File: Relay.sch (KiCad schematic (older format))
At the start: 0 parts

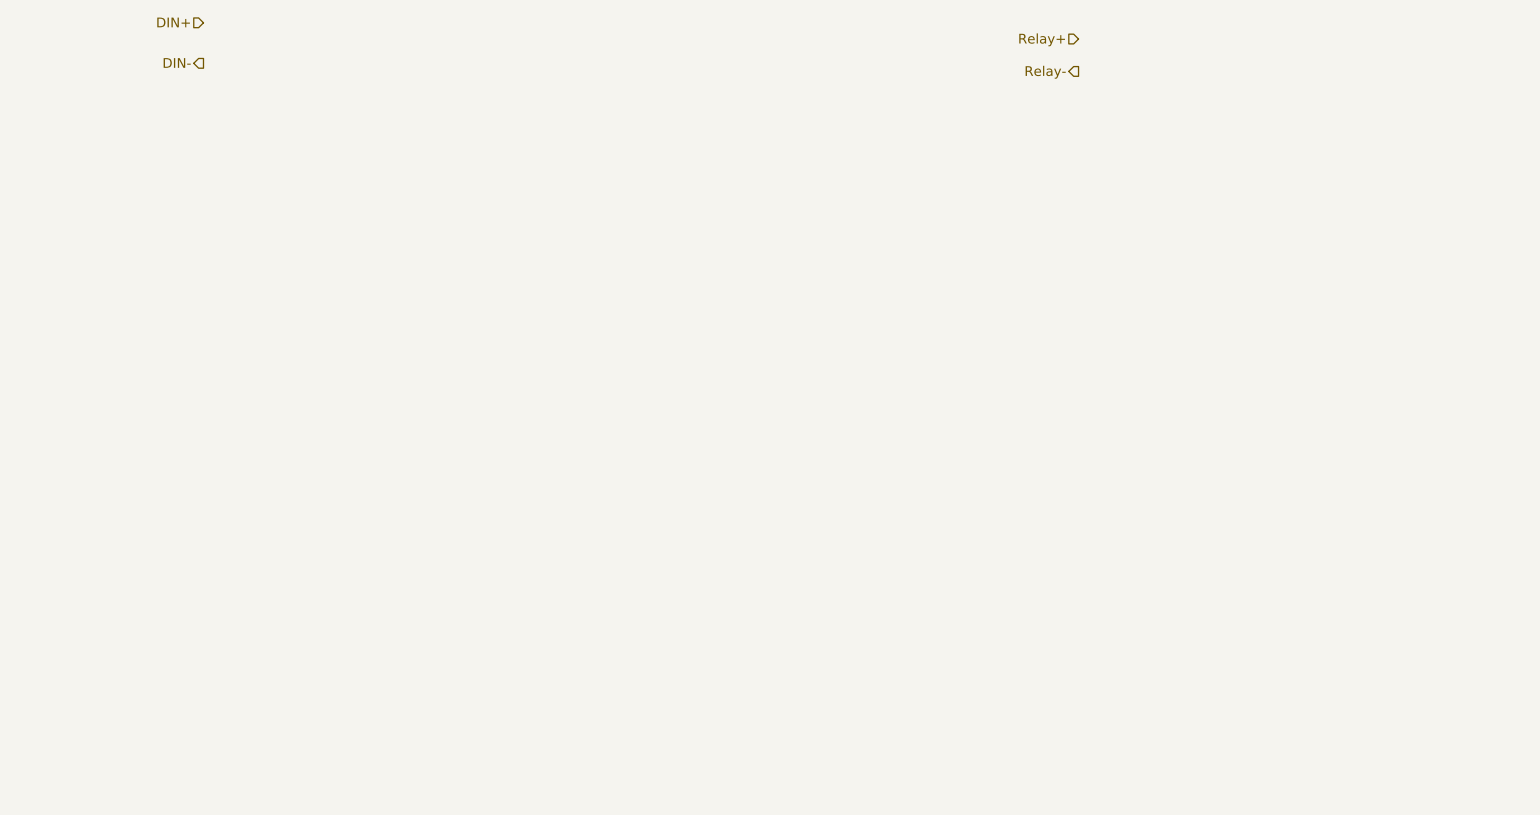
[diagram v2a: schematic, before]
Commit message: Completed LED Driver Video + Power Module
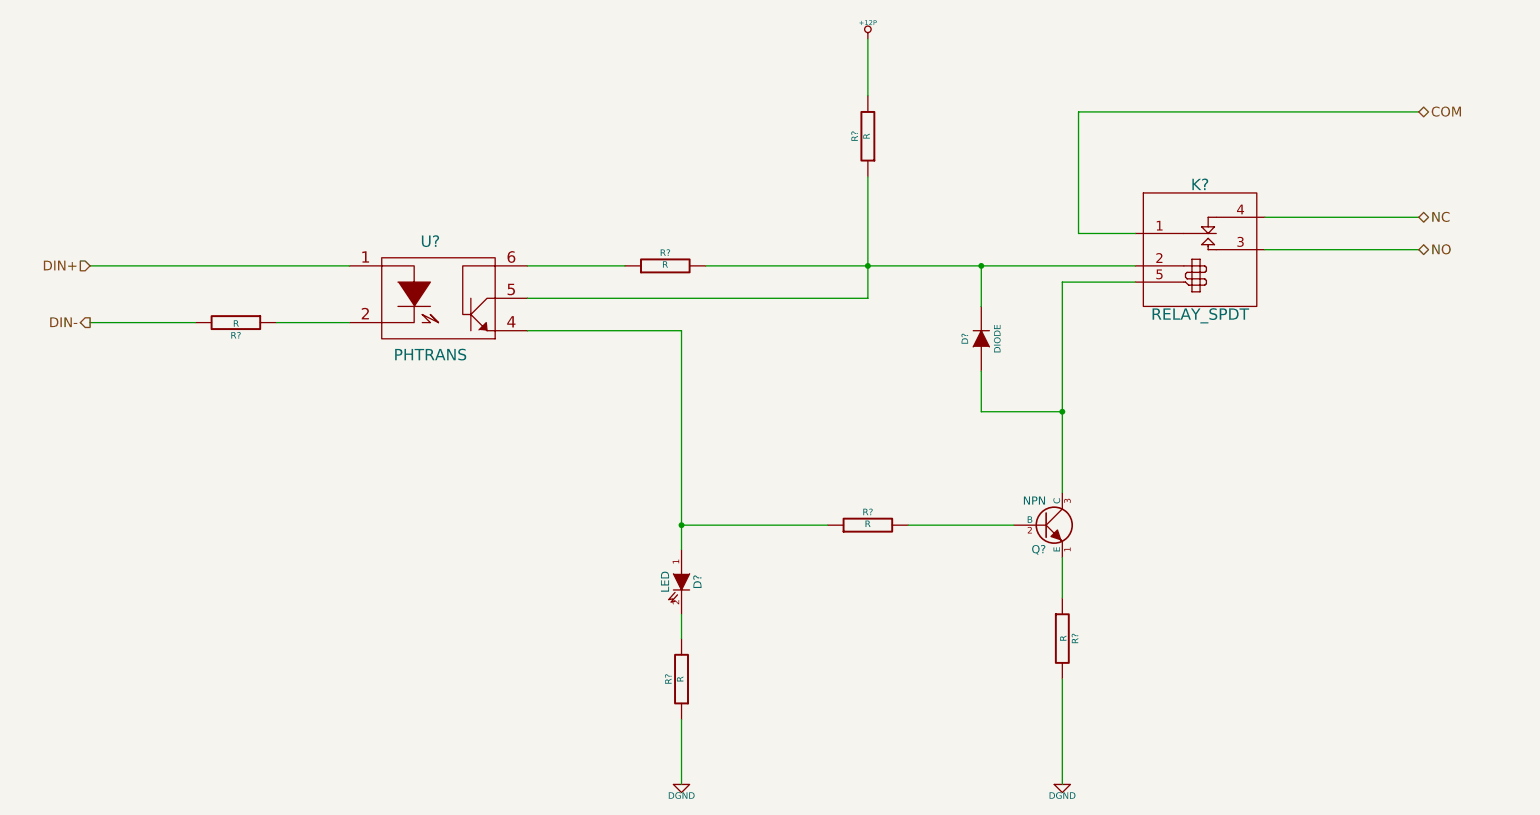
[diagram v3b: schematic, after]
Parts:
- added D?: LED, ~, symbol LED
- added D?: DIODE, ~, symbol DIODE
- added K?: RELAY_SPDT, ~, symbol RELAY_SPDT
- added Q?: NPN, ~, symbol NPN
- added R? (x6): R, ~, symbol R
- added U?: PHTRANS, ~, symbol PHTRANS
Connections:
- net DIN+: now also U?.1
- net DIN-: now also R?.2
- new net: R?.1, U?.2
- new net: D?.1 (A), R?.1, U?.4
- new net: D?.2 (K), K?.2 (COIL+), R?.1, R?.2, U?.5
- new net: R?.1, U?.6
- new net: Q?.2 (B), R?.2
- new net: Q?.1 (E), R?.1
- new net: D?.1 (A), K?.5 (COIL-), Q?.3 (C)
- new net: D?.2 (K), R?.2
- new net +12P: R?.2
- new net COM: K?.1 (COM)
- new net DGND: R?.1, R?.2
- new net NC: K?.4 (NC)
- new net NO: K?.3 (NO)
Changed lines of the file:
@@
 LIBS:contrib
 LIBS:valves
+LIBS:BenchBudEE_Parts
 LIBS:BenchBudEE-cache
 EELAYER 27 0
@@
 $Descr A4 11693 8268
 encoding utf-8
-Sheet 4 8
+Sheet 8 9
 Title ""
-Date "6 feb 2014"
+Date "10 feb 2014"
 Rev ""
 Comp ""
@@
 Comment4 ""
 $EndDescr
-Text HLabel 2250 2050 0    60   Input ~ 0
+Text HLabel 1550 3550 0    60   Input ~ 0
 DIN+
-Text HLabel 2250 2300 0    60   Output ~ 0
+Text HLabel 1550 3900 0    60   Output ~ 0
 DIN-
-Text HLabel 7650 2150 0    60   Input ~ 0
-Relay+
-Text HLabel 7650 2350 0    60   Output ~ 0
-Relay-
+Text HLabel 9750 3450 2    60   BiDi ~ 0
+NO
+Text HLabel 9750 3250 2    60   BiDi ~ 0
+NC
+$Comp
+L PHTRANS U?
+U 1 1 52F65C85
+P 3700 3750
+F 0 "U?" H 3650 4100 70  0000 C CNN
+F 1 "PHTRANS" H 3650 3400 70  0000 C CNN
+F 2 "~" H 3700 3750 60  0000 C CNN
+F 3 "~" H 3700 3750 60  0000 C CNN
+	1    3700 3750
+	1    0    0    -1
+$EndComp
+$Comp
+L R R?
+U 1 1 52F65C9E
+P 6350 5150
+F 0 "R?" V 6430 5150 40  0000 C CNN
+F 1 "R" V 6357 5151 40  0000 C CNN
+F 2 "~" V 6280 5150 30  0000 C CNN
+F 3 "~" H 6350 5150 30  0000 C CNN
+	1    6350 5150
+	0    -1   -1   0
+$EndComp
+$Comp
+L NPN Q?
+U 1 1 52F65CAD
+P 7450 5150
+F 0 "Q?" H 7450 5000 50  0000 R CNN
+F 1 "NPN" H 7450 5300 50  0000 R CNN
+F 2 "~" H 7450 5150 60  0000 C CNN
+F 3 "~" H 7450 5150 60  0000 C CNN
+	1    7450 5150
+	1    0    0    -1
+$EndComp
+$Comp
+L LED D?
+U 1 1 52F65CBC
+P 5200 5500
+F 0 "D?" H 5200 5600 50  0000 C CNN
+F 1 "LED" H 5200 5400 50  0000 C CNN
+F 2 "~" H 5200 5500 60  0000 C CNN
+F 3 "~" H 5200 5500 60  0000 C CNN
+	1    5200 5500
+	0    1    1    0
+$EndComp
+$Comp
+L RELAY_SPDT K?
+U 1 1 52F663F3
+P 8400 3300
+F 0 "K?" H 8400 3550 70  0000 C CNN
+F 1 "RELAY_SPDT" H 8400 2750 70  0000 C CNN
+F 2 "~" H 8400 3300 60  0000 C CNN
+F 3 "~" H 8400 3300 60  0000 C CNN
+	1    8400 3300
+	1    0    0    -1
+$EndComp
+Text HLabel 9750 2600 2    60   BiDi ~ 0
+COM
+$Comp
+L R R?
+U 1 1 52F665DD
+P 7550 5850
+F 0 "R?" V 7630 5850 40  0000 C CNN
+F 1 "R" V 7557 5851 40  0000 C CNN
+F 2 "~" V 7480 5850 30  0000 C CNN
+F 3 "~" H 7550 5850 30  0000 C CNN
+	1    7550 5850
+	1    0    0    -1
+$EndComp
+$Comp
+L DGND #PWR?
+U 1 1 52F665ED
+P 7550 6750
+F 0 "#PWR?" H 7550 6750 40  0001 C CNN
+F 1 "DGND" H 7550 6680 40  0000 C CNN
+F 2 "" H 7550 6750 60  0000 C CNN
+F 3 "" H 7550 6750 60  0000 C CNN
+	1    7550 6750
+	1    0    0    -1
+$EndComp
+$Comp
+L R R?
+U 1 1 52F66784
+P 6350 2750
+F 0 "R?" V 6430 2750 40  0000 C CNN
+F 1 "R" V 6357 2751 40  0000 C CNN
+F 2 "~" V 6280 2750 30  0000 C CNN
+F 3 "~" H 6350 2750 30  0000 C CNN
+	1    6350 2750
+	-1   0    0    1
+$EndComp
+$Comp
+L R R?
+U 1 1 52F66924
+P 5100 3550
+F 0 "R?" V 5180 3550 40  0000 C CNN
+F 1 "R" V 5107 3551 40  0000 C CNN
+F 2 "~" V 5030 3550 30  0000 C CNN
+F 3 "~" H 5100 3550 30  0000 C CNN
+	1    5100 3550
+	0    -1   -1   0
+$EndComp
+$Comp
+L R R?
+U 1 1 52F66991
+P 5200 6100
+F 0 "R?" V 5280 6100 40  0000 C CNN
+F 1 "R" V 5207 6101 40  0000 C CNN
+F 2 "~" V 5130 6100 30  0000 C CNN
+F 3 "~" H 5200 6100 30  0000 C CNN
+	1    5200 6100
+	-1   0    0    1
+$EndComp
+Wire Wire Line
+	9750 2600 7650 2600
+Wire Wire Line
+	7650 2600 7650 3350
+Wire Wire Line
+	7650 3350 8000 3350
+Wire Wire Line
+	9750 3250 8800 3250
+Wire Wire Line
+	8800 3450 9750 3450
+Wire Wire Line
+	8000 3650 7550 3650
+Wire Wire Line
+	7550 3650 7550 4950
+Wire Wire Line
+	7550 6750 7550 6100
+Wire Wire Line
+	7550 5600 7550 5350
+Wire Wire Line
+	6600 5150 7250 5150
+Wire Wire Line
+	6350 2500 6350 2150
+Wire Wire Line
+	6350 3000 6350 3750
+Wire Wire Line
+	4850 3550 4250 3550
+Wire Wire Line
+	5350 3550 8000 3550
+Wire Wire Line
+	6350 3750 4250 3750
+Connection ~ 6350 3550
+Wire Wire Line
+	5200 3950 5200 5300
+Wire Wire Line
+	5200 5850 5200 5700
+$Comp
+L DGND #PWR?
+U 1 1 52F669C7
+P 5200 6750
+F 0 "#PWR?" H 5200 6750 40  0001 C CNN
+F 1 "DGND" H 5200 6680 40  0000 C CNN
+F 2 "" H 5200 6750 60  0000 C CNN
+F 3 "" H 5200 6750 60  0000 C CNN
+	1    5200 6750
+	1    0    0    -1
+$EndComp
+Wire Wire Line
+	5200 6750 5200 6350
+Wire Wire Line
+	1550 3550 3150 3550
+$Comp
+L R R?
+U 1 1 52F66A05
+P 2450 3900
+F 0 "R?" V 2530 3900 40  0000 C CNN
+F 1 "R" V 2457 3901 40  0000 C CNN
+F 2 "~" V 2380 3900 30  0000 C CNN
+F 3 "~" H 2450 3900 30  0000 C CNN
+	1    2450 3900
+	0    1    1    0
+$EndComp
+Wire Wire Line
+	2700 3900 3150 3900
+Wire Wire Line
+	2200 3900 1550 3900
+Wire Wire Line
+	4250 3950 5200 3950
+Wire Wire Line
+	5200 5150 6100 5150
+Connection ~ 5200 5150
+$Comp
+L DIODE D?
+U 1 1 52F66DA7
+P 7050 4000
+F 0 "D?" H 7050 4100 40  0000 C CNN
+F 1 "DIODE" H 7050 3900 40  0000 C CNN
+F 2 "~" H 7050 4000 60  0000 C CNN
+F 3 "~" H 7050 4000 60  0000 C CNN
+	1    7050 4000
+	0    -1   -1   0
+$EndComp
+Wire Wire Line
+	7050 3800 7050 3550
+Connection ~ 7050 3550
+Wire Wire Line
+	7050 4200 7050 4450
+Wire Wire Line
+	7050 4450 7550 4450
+Connection ~ 7550 4450
+$Comp
+L +12P #PWR?
+U 1 1 52F6868D
+P 6350 2150
+F 0 "#PWR?" H 6350 2120 30  0001 C CNN
+F 1 "+12P" H 6350 2250 30  0000 C CNN
+F 2 "" H 6350 2150 60  0000 C CNN
+F 3 "" H 6350 2150 60  0000 C CNN
+	1    6350 2150
+	1    0    0    -1
+$EndComp
 $EndSCHEMATC

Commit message: Completed Arduino Module Video
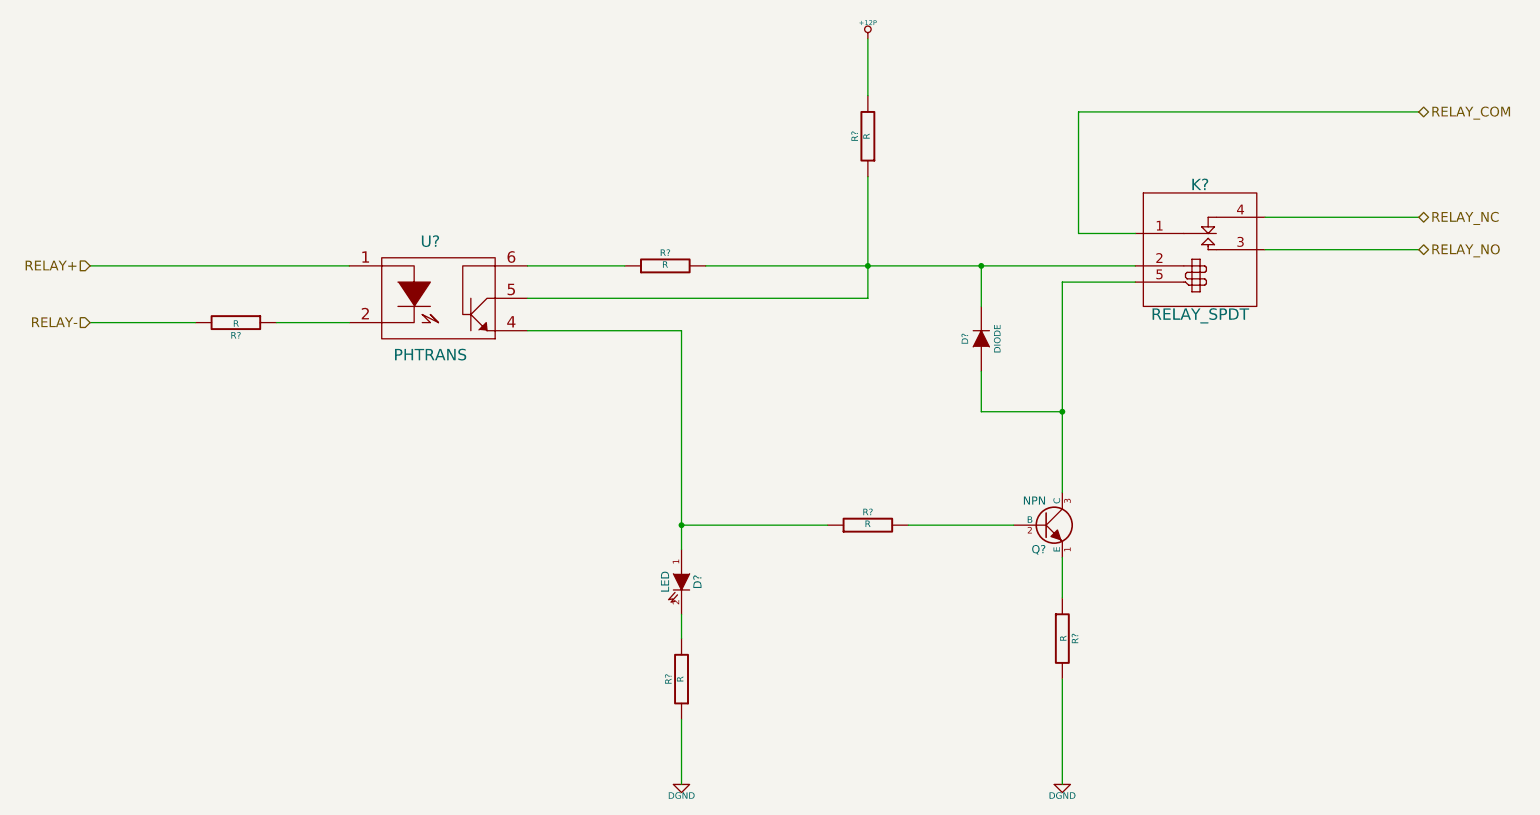
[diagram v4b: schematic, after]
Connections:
- net COM renamed RELAY_COM
- net DIN+ renamed RELAY+
- net DIN- renamed RELAY-
- net NC renamed RELAY_NC
- net NO renamed RELAY_NO
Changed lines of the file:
@@
 $Descr A4 11693 8268
 encoding utf-8
-Sheet 8 9
+Sheet 7 9
 Title ""
-Date "10 feb 2014"
+Date "11 feb 2014"
 Rev ""
 Comp ""
@@
 $EndDescr
 Text HLabel 1550 3550 0    60   Input ~ 0
-DIN+
-Text HLabel 1550 3900 0    60   Output ~ 0
-DIN-
+RELAY+
+Text HLabel 1550 3900 0    60   Input ~ 0
+RELAY-
 Text HLabel 9750 3450 2    60   BiDi ~ 0
-NO
+RELAY_NO
 Text HLabel 9750 3250 2    60   BiDi ~ 0
-NC
+RELAY_NC
 $Comp
 L PHTRANS U?
@@
 $EndComp
 Text HLabel 9750 2600 2    60   BiDi ~ 0
-COM
+RELAY_COM
 $Comp
 L R R?
